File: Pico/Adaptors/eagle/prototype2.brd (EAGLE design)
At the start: 45.8 x 20.7 mm, 13 parts, among them J1 JST-2P-SMD-PW-3410050P1

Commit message: a full panel
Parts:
- added JP12, JP13, JP14: (no value), pinhead-2:1X09-S
- JP1, JP10, JP11, JP2, JP5, JP6, JP7, JP8, JP9: device pinhead-2:1X08-S -> pinhead-2:1X09-S
- U$1: value ESPRUINO_PICO_SMD -> ESPRUINO_PICO_0.1; device espruino_pico:ESPRUINO_PICO_SMD -> espruino_pico:ESPRUINO_PICO_0.1
- moved JP1 25.4 mm to (1.27, 11.4)
- moved JP5 25.4 mm to (3.81, 11.4)
- moved JP6 25.4 mm to (6.35, 11.4)
- moved JP7 25.4 mm to (8.89, 11.4)
- moved JP8 25.4 mm to (11.4, 11.4)
- moved JP9 25.4 mm to (14.0, 11.4)
- moved JP3 24.1 mm to (34.3, 11.4), turned to 270 degrees
- moved J1 22.5 mm to (25.4, 3.81), turned to 0 degrees
- moved JP2 12.8 mm to (36.8, 11.4)
- moved JP4 11.4 mm to (16.5, 11.4), turned to 270 degrees
- moved U$1 10.2 mm to (25.4, 8.89), turned to 270 degrees
- moved JP11 2.84 mm to (41.9, 11.4)
- moved JP10 2.84 mm to (39.4, 11.4)
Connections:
- removed net N$1: JP2.2, U$1.A3
- removed net N$2: JP2.3, U$1.A2
- removed net N$24: JP2.1, U$1.A4
- removed net N$3: JP2.4, U$1.A1
- removed net N$4: JP2.5, U$1.A0
- removed net N$5: JP2.6, U$1.A10
- removed net N$6: JP2.7, U$1.B9
- removed net N$9: JP2.8, U$1.B8
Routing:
- net GND: track 20.2 -> 38.6 mm, vias 3 -> 2
- net N$15: track 13.4 -> 21.8 mm
- net N$1: track 7.86 -> 0.00 mm
- net N$6: track 7.86 -> 0.00 mm
- net N$9: track 5.57 -> 0.00 mm
- net N$24: track 5.57 -> 0.00 mm
- net N$5: track 3.78 -> 0.00 mm
- net N$2: track 3.78 -> 0.00 mm
- net N$4: track 2.80 -> 0.00 mm
- net N$3: track 2.80 -> 0.00 mm
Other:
- board size 45.8 x 20.7 mm -> 50.8 x 22.9 mm

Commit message: minor board tweaks
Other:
- board text added: "Pico This Side"
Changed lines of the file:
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@@
 <wire x1="50.8" y1="22.86" x2="0" y2="22.86" width="0" layer="20"/>
 <wire x1="0" y1="22.86" x2="0" y2="0" width="0" layer="20"/>
+<text x="29.21" y="19.939" size="0.8128" layer="25" rot="R270">Pico This Side</text>
 </plain>
 <attributes>

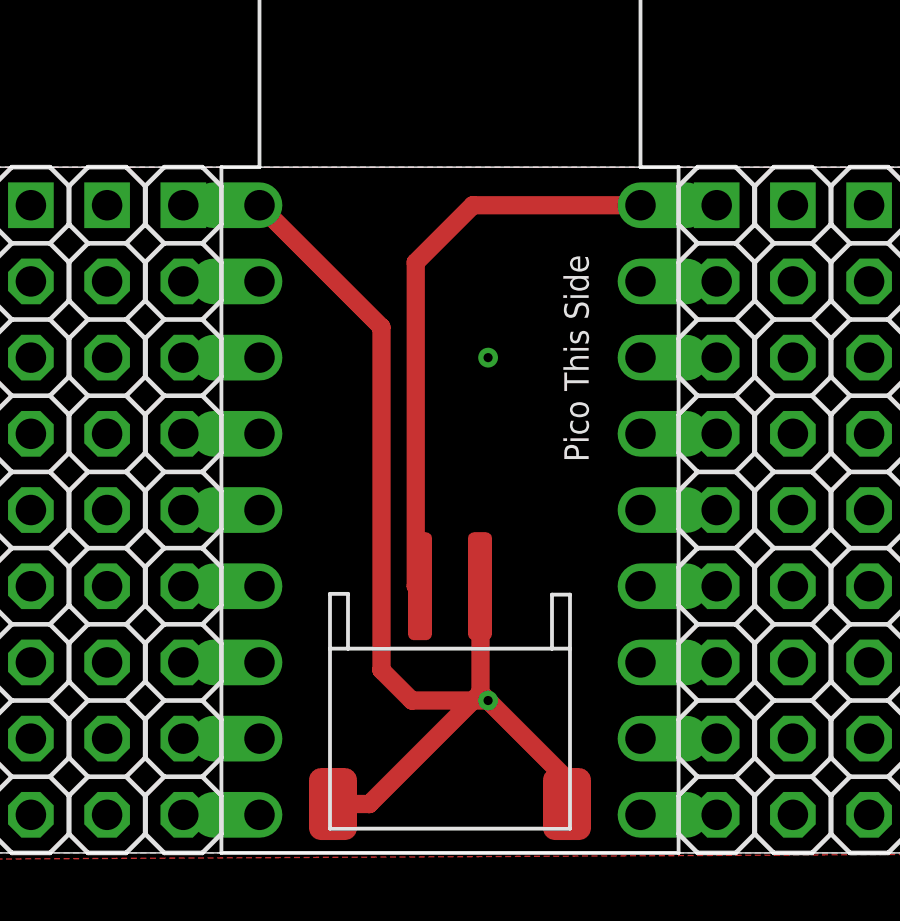
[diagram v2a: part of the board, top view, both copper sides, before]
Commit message: Added battery charger pads to proto headers
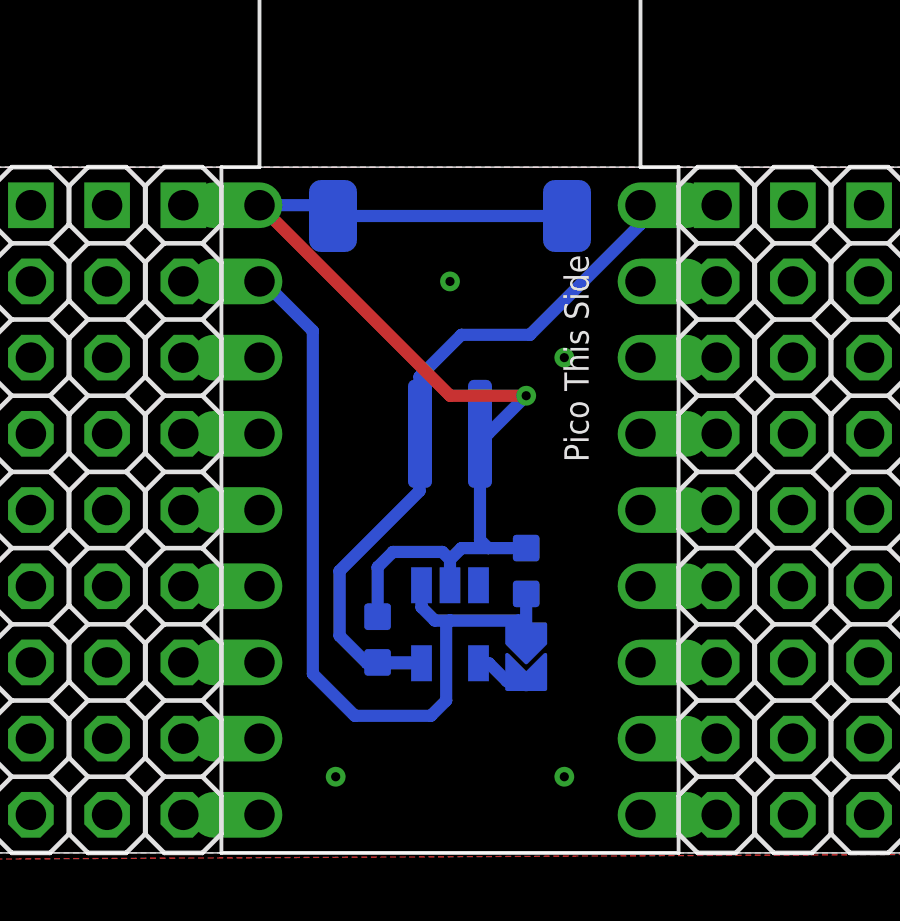
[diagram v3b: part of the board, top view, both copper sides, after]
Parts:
- removed J1: JST-2P-SMD-PW-3410050P1, OPL Eagle Library:2P-SMD-2.0-90D
- added C1, C2: 100nF, OPL5:C0603
- added J2: (no value), OPL Eagle Library:2P-SMD-2.0-90D
- added U$4: SOLDERJUMPER, solder_jumper:SOLDERJUMPER
- added U3: MAX1551, template:SOT23-5
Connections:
- removed net 5V: JP4.2, U$1.5V
- removed net N$15: J1.+, JP3.1, U$1.BAT
- new net BAT: C1.1, J2.+, JP3.1, U$1.BAT, U3.5
- new net N$2: U$4.P$1, U3.4
- new net VIN: C2.1, JP4.2, U$1.5V, U$4.P$2, U3.1
- net GND: now also C1.2, C2.2, J2.-, J2.3, J2.4, U3.2; no longer J1.-, J1.3, J1.4
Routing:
- net VIN: track 0.00 -> 30.0 mm
- net BAT: track 0.00 -> 27.0 mm
- net N$15: track 21.8 -> 0.00 mm
- net 5V: track 2.54 -> 0.00 mm
- net N$2: track 0.00 -> 1.89 mm
- net GND: track 38.6 -> 38.4 mm, vias 2 -> 5
